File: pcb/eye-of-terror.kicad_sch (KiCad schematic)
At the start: 8 parts, among them J1 Conn_01x02_Socket, J2 G-Switch GT-USB-7055E, U1 RP2350B, U2 TD1660, U3 AP63205WU-7, U4 LSM6DS3

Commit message: all components added to schematic
still need to add GPIO pin labels.
next step after that is to verify footprints for everything.
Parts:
- added C1, C39: 10uF, symbol Device:C_Small
- added C10, C11, C14, C15, C17, C2, C21, C22, C23, C24, C25, C26, C27, C28, C29, C9: 100nF, symbol Device:C_Small
- added C12, C13: 15pF, symbol Device:C_Small
- added C16, C18, C19, C20, C8: 4.7uF, symbol Device:C_Small
- added C3, C4, C7: 22uF, symbol Device:C_Small
- added C30, C36, C37, C38: 0.1uF, symbol Device:C_Small
- added C31, C34, C35: 1uF, symbol Device:C_Small
- added C32: 47nF, 47nF, symbol Device:C_Small
- added C33: 1uF, 47nF, symbol Device:C_Small
- added C5: 680pF, symbol Device:C_Small
- added C6: 68pF, symbol Device:C_Small
- added D1: SM6T30A, Diode_SMD:D_SMB, symbol Diode:SM6T30A
- added D2: SS36, Diode_SMD:D_SMA, symbol Diode:SS36
- added D3, D5, D7: GREEN, symbol Device:LED
- added D4, D6, D8: BLUE, symbol Device:LED
- added J3, J4: Conn_01x04, symbol Connector_Generic:Conn_01x04
- added J5: Conn_01x03, symbol Connector_Generic:Conn_01x03
- added J6: Conn_01x02_Socket, Connector_AMASS:AMASS_XT60-M_1x02_P7.20mm_Vertical, symbol Connector:Conn_01x02_Socket
- added JP1, JP10, JP11, JP12, JP13, JP14, JP15, JP2, JP3, JP4, JP5, JP6, JP7, JP8, JP9: SolderJumper_2_Bridged, symbol Jumper:SolderJumper_2_Bridged
- added L1: 4.7uH, symbol Device:L_Small
- added L2: 10uH, symbol Device:L_Small
- added L3: L_Small, ABRACON-AOTA-B201610S3R3-101-T:ABRACON-AOTA-B201610S3R3-101-T, symbol Device:L_Small
- added L4: MOTOR_A, symbol Device:L_45deg
- added L5: MOTOR_C, symbol Device:L_45deg
- added L6: MOTOR_B, symbol Device:L
- added Q1, Q2, Q3, Q4, Q5, Q6: IPT020N10N3, Package_TO_SOT_SMD:Infineon_PG-HSOF-8-1_ThermalVias, symbol Transistor_FET:IPT020N10N3
- added R10, R11, R15, R22, R8: 1k, symbol Device:R_Small_US
- added R12: 33, symbol Device:R_Small_US
- added R13, R14: 27, symbol Device:R_Small_US
- added R16, R21, R24, R9: 10k, symbol Device:R_Small_US
- added R17, R18, R19: 1m, symbol Device:R_Small_US
- added R20: 68k, symbol Device:R_Small_US
- added R23: 1.5k, symbol Device:R_Small_US
- added R25, R26, R27, R28, R29, R30: TBD, symbol Device:R_Small_US
- added R3: 1M, symbol Device:R_Small_US
- added R4: 150k, symbol Device:R_Small_US
- added R5: 43k, symbol Device:R_Small_US
- added R6: 22k, symbol Device:R_Small_US
- added R7: 120k, symbol Device:R_Small_US
- added SW1, SW2: SW_Push, symbol Switch:SW_Push
- added U5: W25Q32JVSS, Package_SO:SOIC-8_5.3x5.3mm_P1.27mm, symbol Memory_Flash:W25Q32JVSS
- added U6: ~, radiomaster-rp2:RP2, symbol radiomaster-rp2:RP2
- added U7: DRV8353HRTAR, TI_DRV8353HRTAR:RTA0040B, symbol TI_DRV8353HRTAR:DRV8353HRTAR
- added Y1: ABM8-272-T3, Crystal:Crystal_SMD_3225-4Pin_3.2x2.5mm, symbol Device:Crystal_GND24
- J1: now left out of the parts list
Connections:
- net DGND is gone; now on net AGND: J2.A1/B12 (GND), J2.B1/A12 (GND), R1.1, R2.1, U1.62 (VREG_PGND), U1.81 (GND)
- net PGND is gone; now on net AGND: J1.2 (Pin_2)
- net +BATT: now also U2.7 (VIN), C30.2, C31.2, C36.2, C37.2, C38.2, C39.2, C8.1, D1.1 (A1), J6.2 (Pin_2), Q1.3 (D), Q3.3 (D), Q5.3 (D), R20.1, R3.1, U7.3 (VM), U7.4 (VDRAIN); no longer J1.1 (Pin_1)
- net USB_DM: now also R14.1
- net USB_DP: now also R13.1
- net at U4.1 (SDO/SA0): now also JP4.2 (B)
- net at U4.12 (CS): now also JP7.2 (B)
- net at U4.13 (SCL): now also JP6.2 (B)
- net at U4.14 (SDA): now also JP5.2 (B)
- net AGND: now reaches U4.2 (SDX)
- net AGND: now also U2.5 (GND), U3.4 (GND), U4.3 (SCX), U4.4 (INT1), U4.6 (GND), U4.7 (GND), U4.9 (INT2), C1.2, C10.1, C11.1, C12.1, C13.1, C14.1, C15.1, C16.1, C17.1, C18.1, C19.1, C20.1, C21.1, C22.1, C23.1, C24.1, C25.1, C26.1, C27.1, C28.1, C29.1, C3.2, C30.1, C33.1, C34.1, C35.1, C36.1, C37.1, C38.1, C39.1, C4.2, C6.2, C7.2, C8.2, D1.2 (A2), D2.2 (A), J3.1 (Pin_1), J4.1 (Pin_1), J5.2 (Pin_2), R10.2, R17.2, R18.2, R19.2, R21.2, R23.2, R24.2, R25.2, R26.2, R27.2, R28.2, R29.2, R30.2, R4.2, R5.2, R6.2, SW1.2, U5.4 (GND), U6.4 (GND), U7.10 (SNA), U7.11 (SNB), U7.20 (SNC), U7.25 (AGND), U7.39 (GND), U7.41 (PAD)
- net +3V3: now reaches U4.5 (VDDIO)
- net +3V3: now also U1.15 (IOVDD), U1.24 (IOVDD), U1.29 (IOVDD), U1.41 (IOVDD), U1.5 (IOVDD), U1.50 (IOVDD), U1.53 (GPIO42_ADC2), U1.59 (ADC_AVDD), U1.60 (IOVDD), U1.64 (VREG_VIN), U1.68 (USB_OTP_VDD), U1.69 (QSPI_IOVDD), U1.76 (IOVDD), U3.1 (FB), U4.8 (VDD), C10.2, C11.2, C14.2, C18.2, C21.2, C22.2, C23.2, C24.2, C25.2, C26.2, C27.2, C28.2, C29.2, C3.1, C35.2, C4.1, J3.2 (Pin_2), J4.2 (Pin_2), L1.2, R12.2, R15.1, R16.1, R24.1, R9.1, U5.8 (VCC), U6.3 (+5V), U7.24 (VREF)
- net RP2_RX: now reaches U1.1 (GPIO4)
- net RP2_RX: now also U6.1 (RX)
- net +1V1: now reaches U1.10 (DVDD), U1.32 (DVDD), U1.51 (DVDD)
- net +1V1: now also U1.65 (VREG_FB), C15.2, C16.2, C17.2, C20.2, L3.1
- net RP2_TX: now reaches U1.2 (GPIO5)
- net RP2_TX: now also U6.2 (TX)
- net XIN: now reaches U1.30 (XIN)
- net XIN: now also C12.2, Y1.1
- net XOUT: now reaches U1.31 (XOUT)
- net XOUT: now also R8.2
- net SWCLK: now reaches U1.33 (SWCLK)
- net SWCLK: now also J5.1 (Pin_1)
- net SWDIO: now reaches U1.34 (SWDIO)
- net SWDIO: now also J5.3 (Pin_3)
- net RUN: now reaches U1.35 (RUN)
- net RUN: now also SW2.1
- net BATT_MON: now reaches U1.49 (GPIO40_ADC0)
- net BATT_MON: now also R20.2, R21.1
- net 5V_MON: now reaches U1.52 (GPIO41_ADC1)
- net 5V_MON: now also R22.2, R23.1
- net SOC: now reaches U1.54 (GPIO43_ADC3)
- net SOC: now also U7.21 (SOC)
- net SOB: now reaches U1.55 (GPIO44_ADC4)
- net SOB: now also U7.22 (SOB)
- net SOA: now reaches U1.56 (GPIO45_ADC5)
- net SOA: now also U7.23 (SOA)
- net at U1.61 (VREG_AVDD): now also C19.2, R12.1
- net at U1.63 (VREG_LX): now also L3.2
- net at U1.66 (USB_DM): now also R14.2
- net at U1.67 (USB_DP): now also R13.2
- net QSPI_SD3: now reaches U1.70 (QSPI_SD3)
- net QSPI_SD3: now also U5.7 (~{HOLD}/~{RESET}/IO_{3})
- net QSPI_SCLK: now reaches U1.71 (QSPI_SCLK)
- net QSPI_SCLK: now also U5.6 (CLK)
- net QSPI_SD0: now reaches U1.72 (QSPI_SD0)
- net QSPI_SD0: now also U5.5 (DI/IO_{0})
- net QSPI_SD2: now reaches U1.73 (QSPI_SD2)
- net QSPI_SD2: now also U5.3 (~{WP}/IO_{2})
- net QSPI_SD1: now reaches U1.74 (QSPI_SD1)
- net QSPI_SD1: now also U5.2 (DO/IO_{1})
- net QSPI_SS: now reaches U1.75 (QSPI_SS)
- net QSPI_SS: now also R11.1
- net GPIO0: now reaches U1.77 (GPIO0)
- net GPIO0: now also JP8.1 (A)
- net at U2.1 (SW): now also C9.2, D2.1 (K), L2.1
- net at U2.2 (EN): now also R3.2
- net at U2.3 (COMP): now also C5.1, C6.1
- net at U2.4 (FB): now also R6.1, R7.1
- net at U2.6 (FREQ): now also R4.1
- net at U2.8 (BST): now also C9.1
- net +5V: now reaches U3.2 (EN)
- net +5V: now also U3.3 (VIN), C1.1, C7.1, L2.2, R22.1, R7.2
- net at U3.5 (SW): now also C2.2, L1.1
- net at U3.6 (BST): now also C2.1
- new net: C13.2, R8.1, Y1.3
- new net: J3.3 (Pin_3), JP1.2 (B)
- new net: J3.4 (Pin_4), JP9.2 (B)
- new net: C5.2, R5.1
- new net: D5.2 (A), JP12.2 (B)
- new net: C34.2, U7.40 (VGLS)
- new net: D8.2 (A), JP15.2 (B)
- new net: D8.1 (K), R30.1
- new net: JP8.2 (B), R9.2, U5.1 (~{CS})
- new net: R10.1, SW2.2
- new net: D3.1 (K), R25.1
- new net: R11.2, SW1.1
- new net: D5.1 (K), R27.1
- new net: D6.1 (K), R28.1
- new net: D6.2 (A), JP13.2 (B)
- new net: D7.2 (A), JP14.2 (B)
- new net: D4.2 (A), JP11.2 (B)
- new net: C33.2, U7.38 (DVDD)
- new net: C31.1, U7.5 (VCP)
- new net: D3.2 (A), JP10.2 (B)
- new net: J4.3 (Pin_3), JP2.2 (B)
- new net: D7.1 (K), R29.1
- new net: C32.1, U7.1 (CPL)
- new net: C32.2, U7.2 (CPH)
- new net: D4.1 (K), R26.1
- new net: J4.4 (Pin_4), JP3.2 (B)
- new net +BATT_RAW: J1.1 (Pin_1), J6.1 (Pin_1)
- new net DRIVER_CIPO: R15.2, U7.27 (SDO)
- new net DRIVER_COPI: U7.28 (SDI)
- new net DRIVER_CS: U7.30 (SCS_N)
- new net DRIVER_ENABLE: U7.31 (ENABLE)
- new net DRIVER_FAULTn: R16.2, U7.26 (FAULT_N)
- new net DRIVER_SCLK: U7.29 (SCLK)
- new net GHA: Q1.1 (G), U7.6 (GHA)
- new net GHB: Q3.1 (G), U7.15 (GHB)
- new net GHC: Q5.1 (G), U7.16 (GHC)
- new net GLA: Q2.1 (G), U7.8 (GLA)
- new net GLB: Q4.1 (G), U7.13 (GLB)
- new net GLC: Q6.1 (G), U7.18 (GLC)
- new net IMU_CIPO: JP4.1 (A)
- new net IMU_COPI: JP5.1 (A)
- new net IMU_CS: JP7.1 (A)
- new net IMU_SCK: JP6.1 (A)
- new net INHA: JP10.1 (A), U7.32 (INHA)
- new net INHB: JP12.1 (A), U7.34 (INHB)
- new net INHC: JP14.1 (A), U7.36 (INHC)
- new net INLA: JP11.1 (A), U7.33 (INLA)
- new net INLB: JP13.1 (A), U7.35 (INLB)
- new net INLC: JP15.1 (A), U7.37 (INLC)
- new net MOT_A: L4.2, L5.2, Q1.2 (S), Q2.3 (D), U7.7 (SHA)
- new net MOT_B: L4.1, L6.2, Q3.2 (S), Q4.3 (D), U7.14 (SHB)
- new net MOT_C: L5.1, L6.1, Q5.2 (S), Q6.3 (D), U7.17 (SHC)
- new net SCL_BOT_IR_TOF: JP3.1 (A)
- new net SCL_TOP_IR_TOF: JP9.1 (A)
- new net SDA_BOT_IR_TOF: JP2.1 (A)
- new net SDA_TOP_IR_TOF: JP1.1 (A)
- new net SPA: Q2.2 (S), R19.1, U7.9 (SPA)
- new net SPB: Q4.2 (S), R17.1, U7.12 (SPB)
- new net SPC: Q6.2 (S), R18.1, U7.19 (SPC)
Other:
- note added: "12 MHz Crystal"
- note added: "Adding jumpers that can be cut later in case the LEDs in parallel cause problems for some reason."
- note added: "Battery Jumper"
- note added: "Battery Monitors"
- note added: "Future-proofing schematic in case it turns out that power ground, digital ground, and analog ground need to be separated and connect together at one point only."
- note added: "Ground Connection"
- note added: "MOSFETs"
- note added: "Motor"
- note added: "Motor LEDs"
- note added: "Push Buttons"
- note added: "RP2 Transceiver"
- note added: "SWD"
- note added: "Secondary Flash"
- note added: "Short these two pins to enable power from battery to the rest of the board. When left open, +BATT_RAW is connected to nothing else, and +BATT is not "live.""
- note added: "TI DRV8353 Gate Driver"
- note added: "This pinout follows Adafruit's STEMMA QT cables."
- moved on the sheet: U1, U2, U3, U4

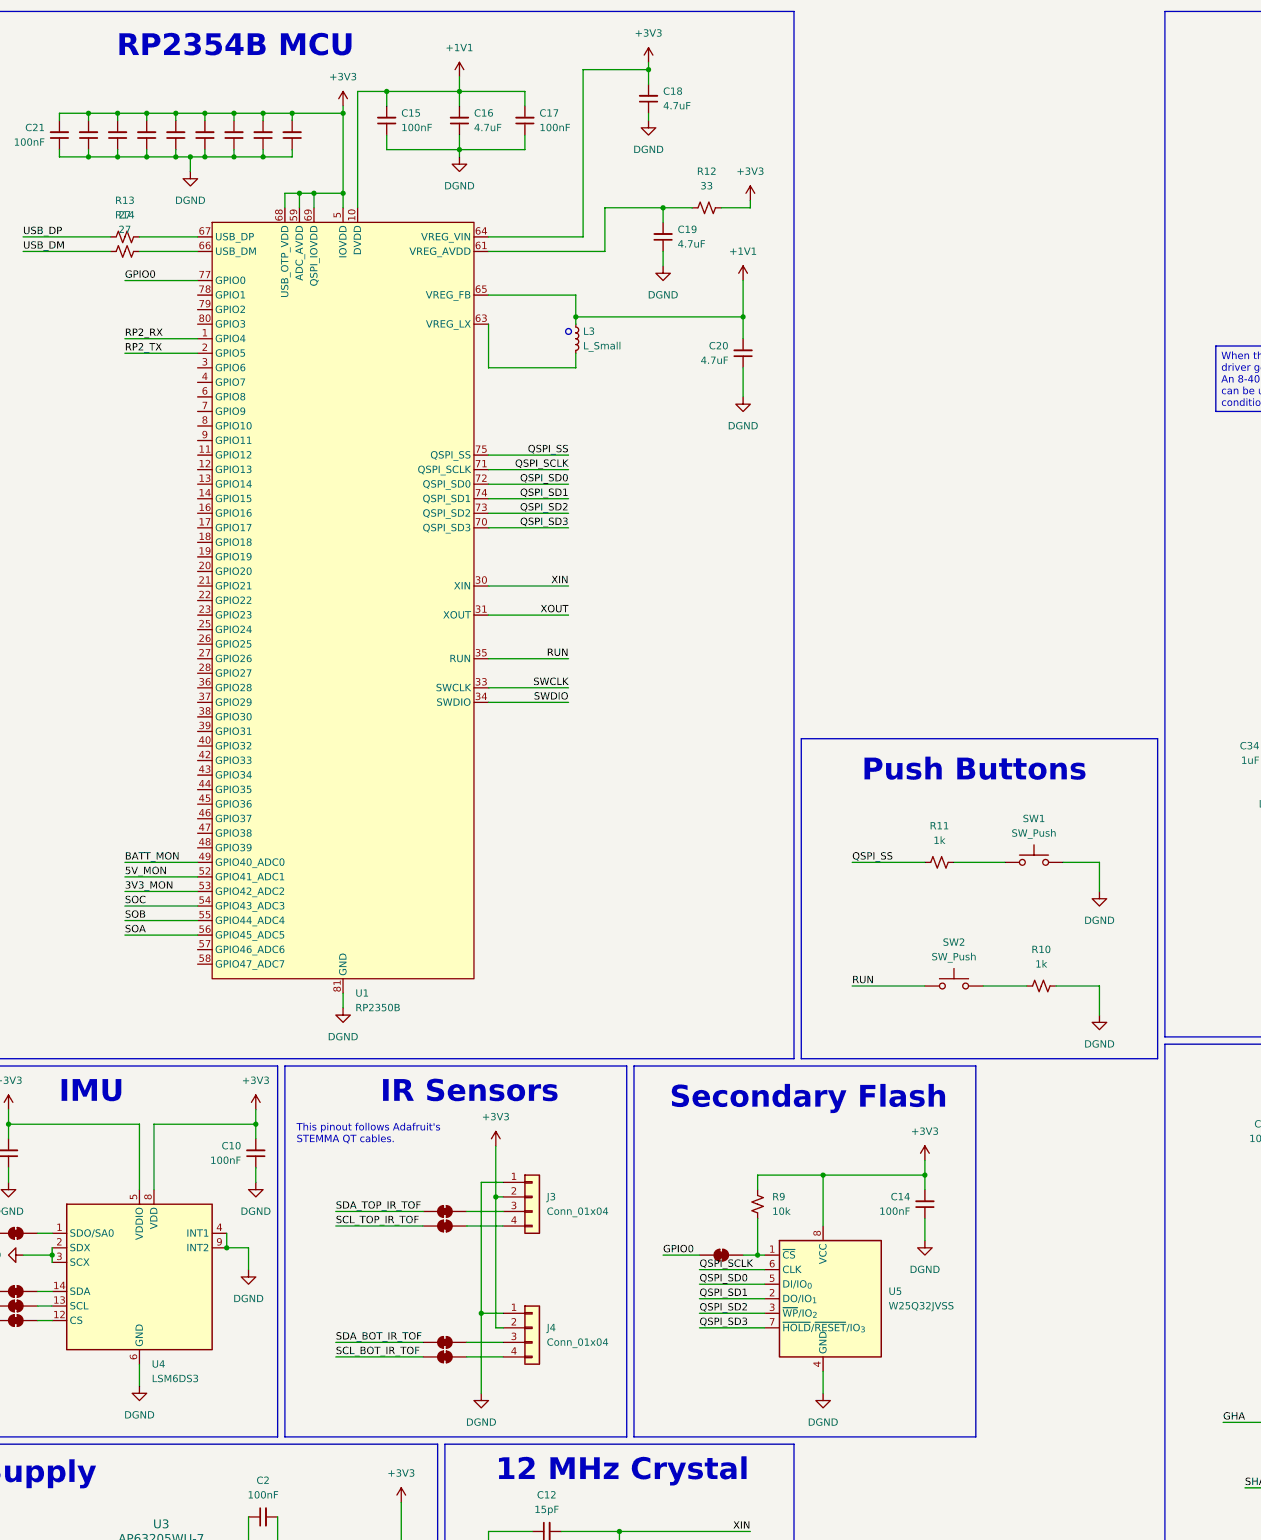
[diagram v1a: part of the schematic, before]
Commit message: added gpio labels and indicator LEDs
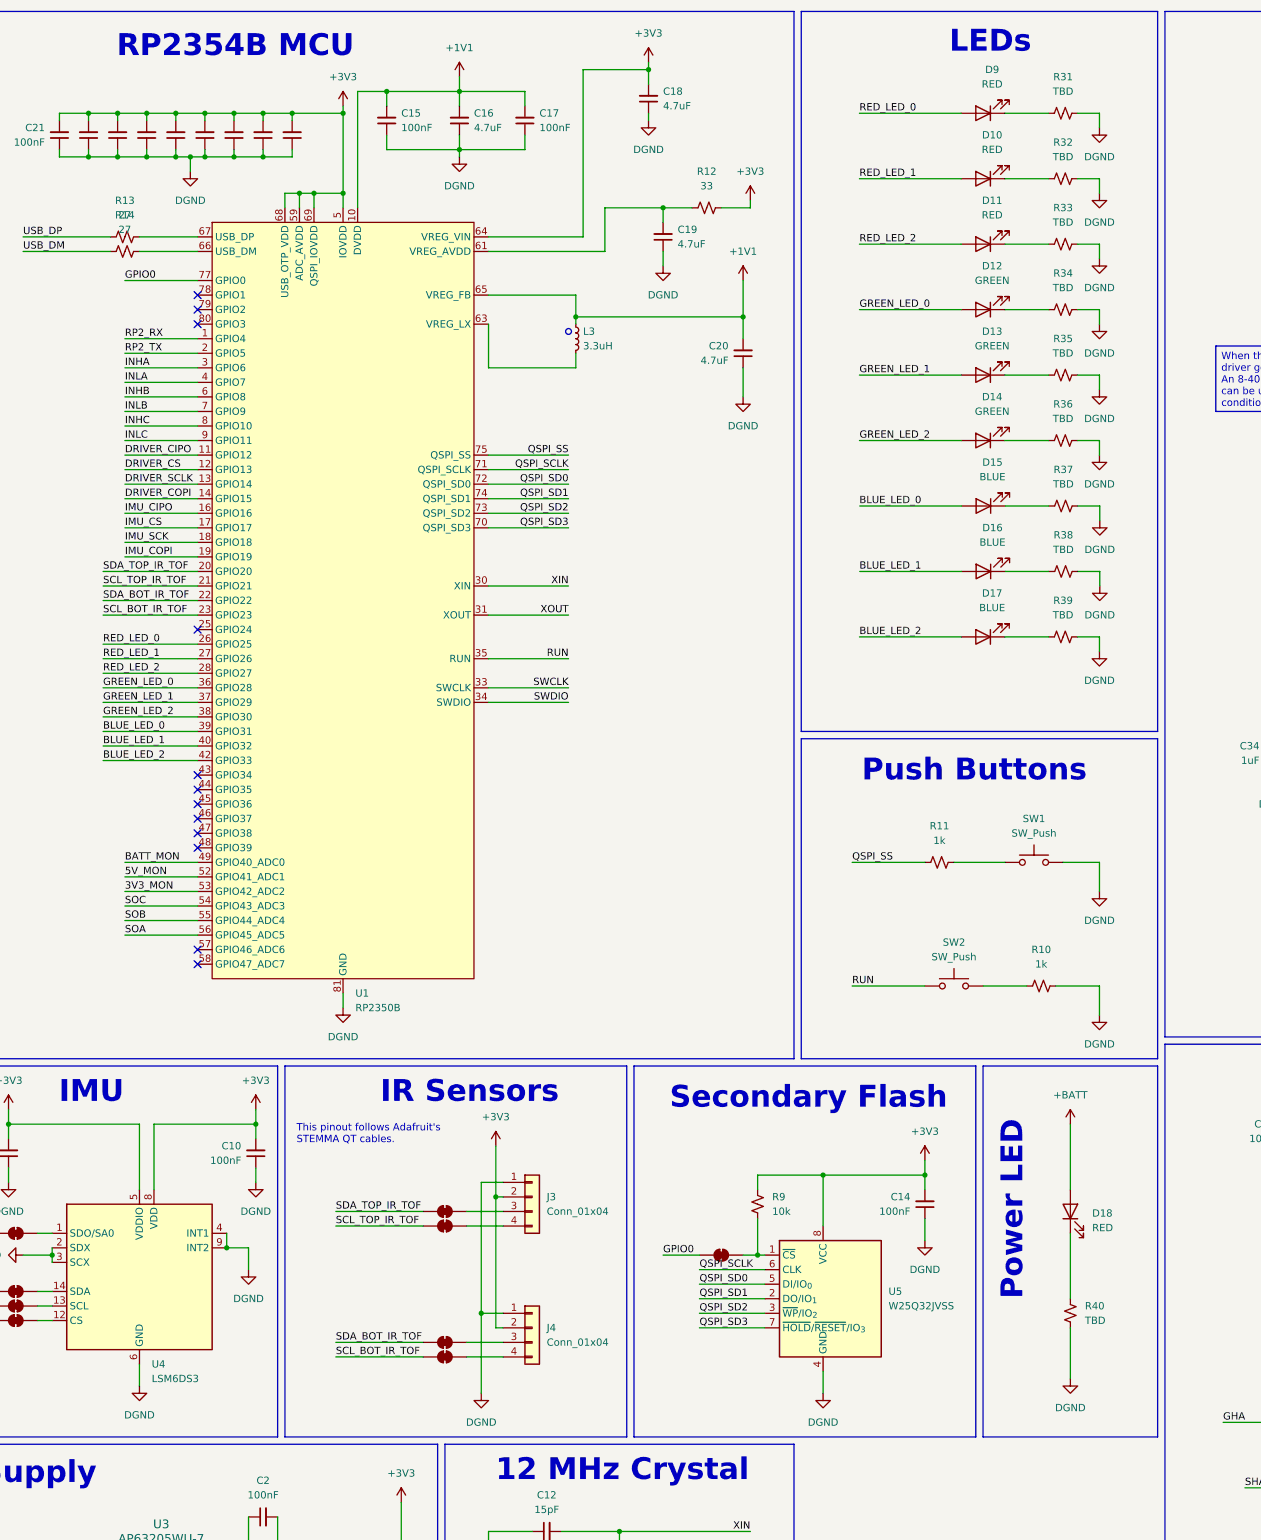
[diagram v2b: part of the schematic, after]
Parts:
- added D10, D11, D18, D9: RED, symbol Device:LED
- added D12, D13, D14: GREEN, symbol Device:LED
- added D15, D16, D17: BLUE, symbol Device:LED
- added R31, R32, R33, R34, R35, R36, R37, R38, R39, R40: TBD, symbol Device:R_Small_US
- L3: value L_Small -> 3.3uH
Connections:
- net +BATT: now also D18.2 (A)
- net AGND: now also R31.2, R32.2, R33.2, R34.2, R35.2, R36.2, R37.2, R38.2, R39.2, R40.1
- net DRIVER_CIPO: now also U1.11 (GPIO12)
- net DRIVER_COPI: now also U1.14 (GPIO15)
- net DRIVER_CS: now also U1.12 (GPIO13)
- net DRIVER_SCLK: now also U1.13 (GPIO14)
- net IMU_CIPO: now also U1.16 (GPIO16)
- net IMU_COPI: now also U1.19 (GPIO19)
- net IMU_CS: now also U1.17 (GPIO17)
- net IMU_SCK: now also U1.18 (GPIO18)
- net INHA: now also U1.3 (GPIO6)
- net INHB: now also U1.6 (GPIO8)
- net INHC: now also U1.8 (GPIO10)
- net INLA: now also U1.4 (GPIO7)
- net INLB: now also U1.7 (GPIO9)
- net INLC: now also U1.9 (GPIO11)
- net SCL_BOT_IR_TOF: now also U1.23 (GPIO23)
- net SCL_TOP_IR_TOF: now also U1.21 (GPIO21)
- net SDA_BOT_IR_TOF: now also U1.22 (GPIO22)
- net SDA_TOP_IR_TOF: now also U1.20 (GPIO20)
- net RED_LED_0: now reaches U1.26 (GPIO25)
- net RED_LED_0: now also D9.2 (A)
- net RED_LED_1: now reaches U1.27 (GPIO26)
- net RED_LED_1: now also D10.2 (A)
- net RED_LED_2: now reaches U1.28 (GPIO27)
- net RED_LED_2: now also D11.2 (A)
- net GREEN_LED_0: now reaches U1.36 (GPIO28)
- net GREEN_LED_0: now also D12.2 (A)
- net GREEN_LED_1: now reaches U1.37 (GPIO29)
- net GREEN_LED_1: now also D13.2 (A)
- net GREEN_LED_2: now reaches U1.38 (GPIO30)
- net GREEN_LED_2: now also D14.2 (A)
- net BLUE_LED_0: now reaches U1.39 (GPIO31)
- net BLUE_LED_1: now reaches U1.40 (GPIO32)
- net BLUE_LED_2: now reaches U1.42 (GPIO33)
- net BLUE_LED_2: now also D17.2 (A)
- new net: D13.1 (K), R35.1
- new net: D16.1 (K), R38.1
- new net: D15.1 (K), R37.1
- new net: D12.1 (K), R34.1
- new net: D17.1 (K), R39.1
- new net: D11.1 (K), R33.1
- new net: D18.1 (K), R40.2
- new net: D9.1 (K), R31.1
- new net: D14.1 (K), R36.1
- new net: D10.1 (K), R32.1
- no-connect marks 2 -> 14
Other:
- note added: "LEDs"
- note added: "Power LED"

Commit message: fixed bugs in schematic, added most footprints
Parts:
- removed L4: MOTOR_A, symbol Device:L_45deg
- removed L5: MOTOR_C, symbol Device:L_45deg
- removed L6: MOTOR_B, symbol Device:L
- added TP1, TP2, TP3: TestPoint, TestPoint:TestPoint_Pad_D2.5mm, symbol Connector:TestPoint
- C10, C11, C14, C15, C16, C17, C18, C19, C2, C20, C21, C22, C23, C24, C25, C26, C27, C28, C29, C3, C31, C34, C35, C4, C6, C7, C8, C9: footprint (none) -> Capacitor_SMD:C_0603_1608Metric
- C12, C13, C5: footprint (none) -> Capacitor_SMD:C_0402_1005Metric
- C30, C36, C37, C38: value 0.1uF -> 100nF; footprint (none) -> Capacitor_SMD:C_0603_1608Metric
- C32: footprint 47nF -> Capacitor_SMD:C_0402_1005Metric
- C33: footprint 47nF -> Capacitor_SMD:C_0603_1608Metric
- D10, D11, D12, D13, D14, D15, D16, D17, D18, D3, D4, D5, D6, D7, D8, D9: footprint (none) -> Diode_SMD:D_1206_3216Metric
- D2: footprint Diode_SMD:D_SMA -> Diode_SMD:D_SMB
- J3, J4, U6: now left out of the parts list
- R1, R10, R11, R12, R13, R14, R15, R16, R2, R21, R22, R24, R4, R8, R9: footprint (none) -> Resistor_SMD:R_0402_1005Metric
- R17, R18, R19: footprint (none) -> Resistor_SMD:R_1206_3216Metric
- R20, R3, R5, R6, R7: footprint (none) -> Resistor_SMD:R_0603_1608Metric
- R23: footprint (none) -> Resistor_SMD:R_1210_3225Metric
- R25, R27, R29, R31, R32, R33, R34, R35, R36: value TBD -> 68; footprint (none) -> Resistor_SMD:R_0402_1005Metric
- R26, R28, R30, R37, R38, R39: value TBD -> 15; footprint (none) -> Resistor_SMD:R_0603_1608Metric
- R40: value TBD -> 1.5k; footprint (none) -> Resistor_SMD:R_1210_3225Metric
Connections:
- net BLUE_LED_0: now also D15.2 (A)
- net BLUE_LED_1: now also D16.2 (A)
- net DRIVER_ENABLE: now also U1.45 (GPIO36)
- net SPA: now also TP1.1
- net SPB: now also TP2.1
- net SPC: now also TP3.1
- net GND: now reaches Y1.2
- net GND: now also Y1.4
- no-connect marks 14 -> 13
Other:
- note removed: "Motor"
- moved on the sheet: D17, D3, D4, D5, D6, D7, D8, R25, R26, R27, R28, R29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
